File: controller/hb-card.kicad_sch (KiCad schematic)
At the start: 12 parts, among them J4 Conn_01x14

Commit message: Controller - More work mainly on layout
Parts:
- R18, R23, R24, R42, R43, R44, R45, R46: footprint Resistor_SMD:R_0402_1005Metric -> Resistor_SMD:R_0805_2012Metric
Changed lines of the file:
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@@
 			)
 		)
-		(property "Footprint" "Resistor_SMD:R_0402_1005Metric"
+		(property "Footprint" "Resistor_SMD:R_0805_2012Metric"
 			(at 77.47 90.17 0)
 			(effects
@@
 			)
 		)
-		(property "Footprint" "Resistor_SMD:R_0402_1005Metric"
+		(property "Footprint" "Resistor_SMD:R_0805_2012Metric"
 			(at 77.47 95.25 0)
 			(effects
@@
 			)
 		)
-		(property "Footprint" "Resistor_SMD:R_0402_1005Metric"
+		(property "Footprint" "Resistor_SMD:R_0805_2012Metric"
 			(at 77.47 67.31 0)
 			(effects
@@
 			)
 		)
-		(property "Footprint" "Resistor_SMD:R_0402_1005Metric"
+		(property "Footprint" "Resistor_SMD:R_0805_2012Metric"
 			(at 77.47 59.69 0)
 			(effects
@@
 			)
 		)
-		(property "Footprint" "Resistor_SMD:R_0402_1005Metric"
+		(property "Footprint" "Resistor_SMD:R_0805_2012Metric"
 			(at 77.47 62.23 0)
 			(effects
@@
 			)
 		)
-		(property "Footprint" "Resistor_SMD:R_0402_1005Metric"
+		(property "Footprint" "Resistor_SMD:R_0805_2012Metric"
 			(at 77.47 92.71 0)
 			(effects
@@
 			)
 		)
-		(property "Footprint" "Resistor_SMD:R_0402_1005Metric"
+		(property "Footprint" "Resistor_SMD:R_0805_2012Metric"
 			(at 77.47 87.63 0)
 			(effects
@@
 			)
 		)
-		(property "Footprint" "Resistor_SMD:R_0402_1005Metric"
+		(property "Footprint" "Resistor_SMD:R_0805_2012Metric"
 			(at 77.47 64.77 0)
 			(effects

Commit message: Controller - some more changes
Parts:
- added C38, C43, C48: 10nF, Capacitor_SMD:C_0402_1005Metric, symbol Device:C_Small
- added C53, C58: 1nF 100VDC, Capacitor_SMD:C_0603_1608Metric, symbol Device:C_Small
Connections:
- net Current_sense_xA: now also C43.1
- net Current_sense_xB: now also C38.1
- net Earth: now also C38.2, C43.2, C48.2, C53.2, C58.2
- net FB_x_FULL_HI: now also C53.1
- net FB_x_FULL_LO: now also C58.1
- net NTC_x: now also C48.1

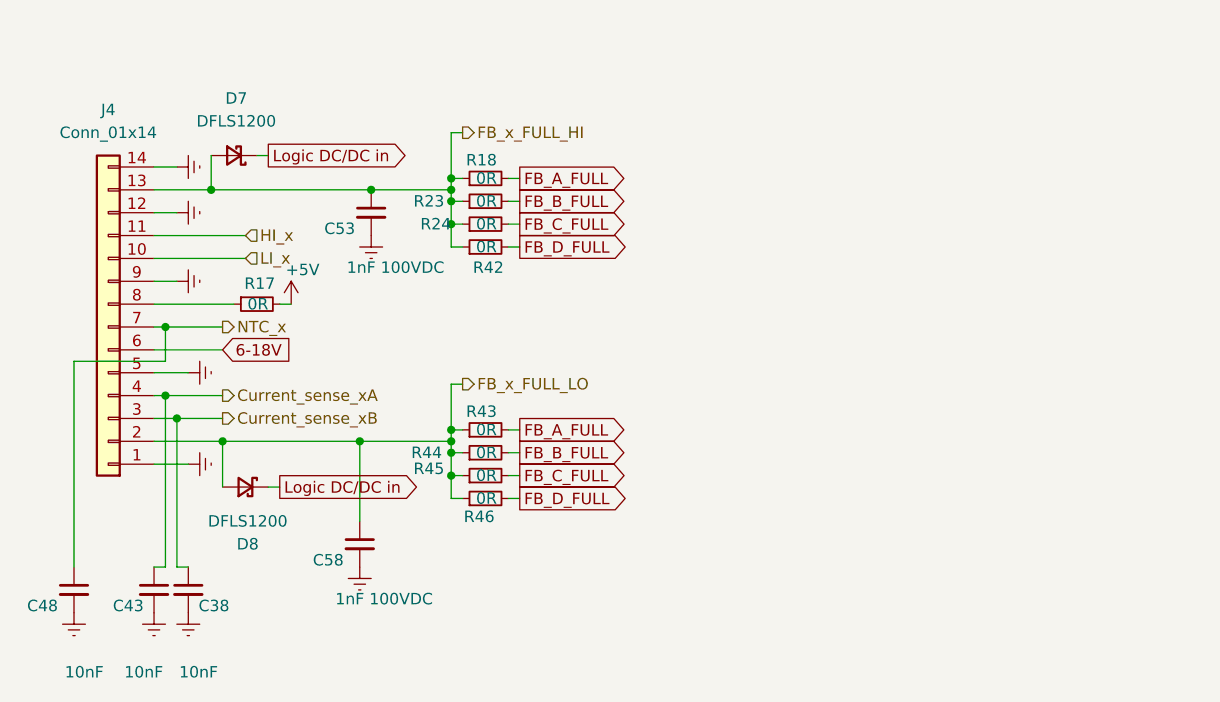
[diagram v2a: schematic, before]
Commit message: Controller - Start work on vbus connection, improve rgb-led placement
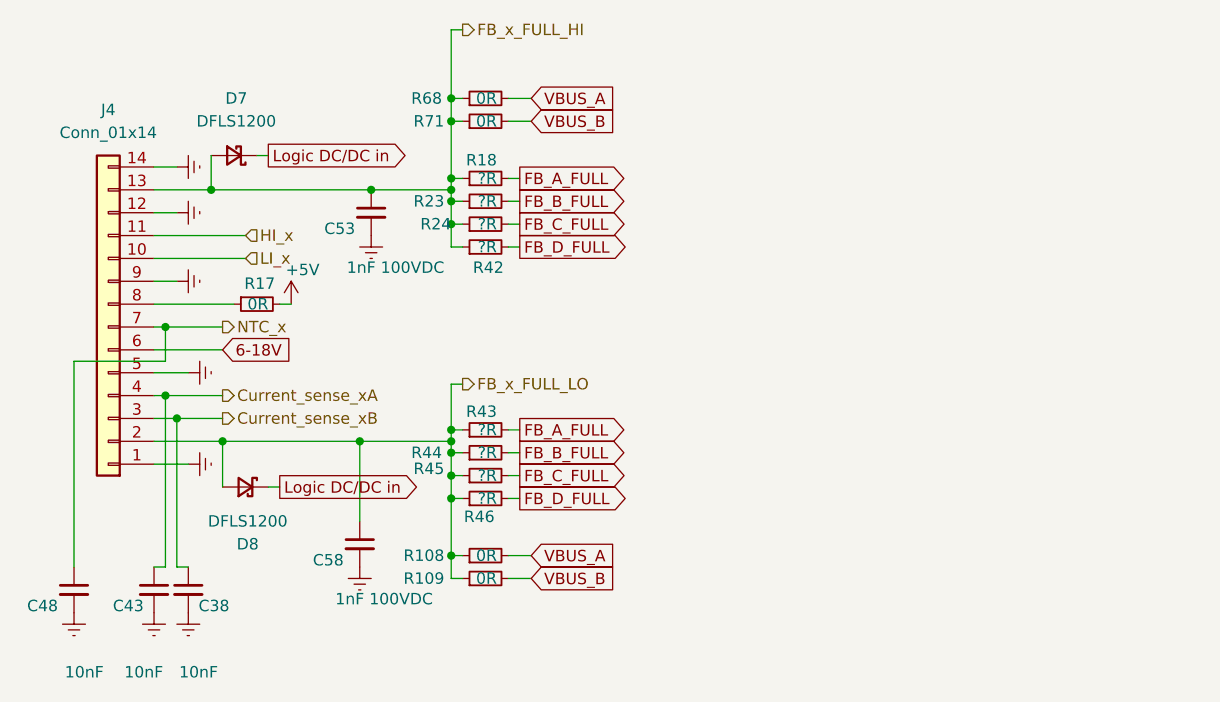
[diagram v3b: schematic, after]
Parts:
- added R108, R109, R68, R71: 0R, Resistor_SMD:R_0805_2012Metric, symbol Device:R_Small
- R18, R23, R24, R42, R43, R44, R45, R46: value 0R -> ?R
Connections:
- net FB_x_FULL_HI: now also R68.1, R71.1
- net FB_x_FULL_LO: now also R108.1, R109.1
- new net VBUS_A: R108.2, R68.2
- new net VBUS_B: R109.2, R71.2

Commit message: Controller - Change current sensor
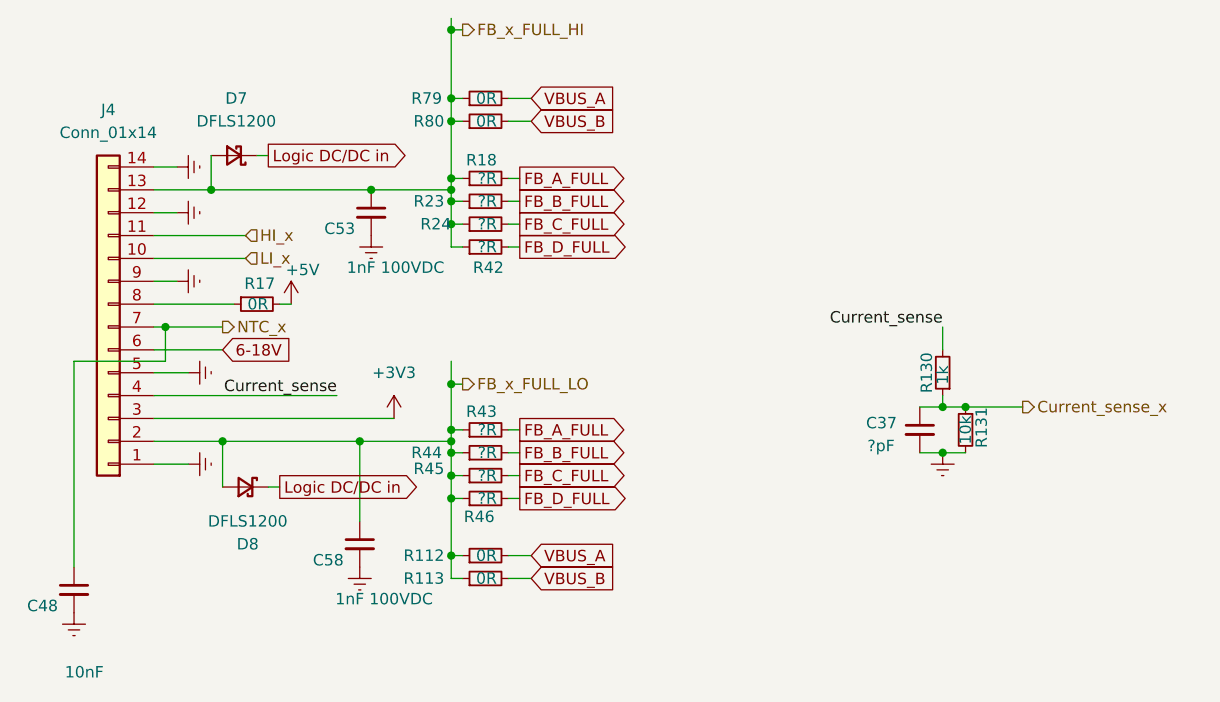
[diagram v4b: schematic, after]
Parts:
- removed C38, C43: 10nF, Capacitor_SMD:C_0402_1005Metric, symbol Device:C_Small
- added C37: ?pF, Capacitor_SMD:C_0402_1005Metric, symbol Device:C_Small
- added R130: 1k, Resistor_SMD:R_0402_1005Metric, symbol Device:R_Small
- added R131: 10k, Resistor_SMD:R_0402_1005Metric, symbol Device:R_Small
- renumbered R108 to R112, R109 to R113, R68 to R79, R71 to R80
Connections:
- net Earth: now also C37.2, R131.2
- net Current_sense_xA renamed Current_sense
- net Current_sense: now also R130.2
- net Current_sense_xB renamed +3V3
- new net Current_sense_x: C37.1, R130.1, R131.1

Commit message: Controller - More routing
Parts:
- removed R131: 10k, Resistor_SMD:R_0402_1005Metric, symbol Device:R_Small
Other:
- moved on the sheet: C37
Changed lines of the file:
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@@
 	)
 	(junction
-		(at 128.27 90.17)
-		(diameter 0)
-		(color 0 0 0 0)
-	)
-	(junction
 		(at 73.66 92.71)
 		(diameter 0)
@@
 	)
 	(junction
-		(at 130.81 85.09)
-		(diameter 0)
-		(color 0 0 0 0)
-	)
-	(junction
 		(at 128.27 85.09)
 		(diameter 0)
@@
 	(wire
 		(pts
-			(xy 128.27 85.09) (xy 130.81 85.09)
+			(xy 128.27 85.09) (xy 137.16 85.09)
 		)
 		(stroke
@@
 	(wire
 		(pts
-			(xy 125.73 90.17) (xy 128.27 90.17)
-		)
-		(stroke
-			(width 0)
-			(type default)
-		)
-	)
-	(wire
-		(pts
 			(xy 74.93 92.71) (xy 73.66 92.71)
 		)
@@
 	(wire
 		(pts
-			(xy 130.81 85.09) (xy 137.16 85.09)
-		)
-		(stroke
-			(width 0)
-			(type default)
-		)
-	)
-	(wire
-		(pts
 			(xy 73.66 87.63) (xy 73.66 88.9)
 		)
@@
 	(wire
 		(pts
-			(xy 125.73 85.09) (xy 128.27 85.09)
-		)
-		(stroke
-			(width 0)
-			(type default)
-		)
-	)
-	(wire
-		(pts
 			(xy 74.93 43.18) (xy 73.66 43.18)
 		)
@@
 	(wire
 		(pts
-			(xy 128.27 90.17) (xy 130.81 90.17)
-		)
-		(stroke
-			(width 0)
-			(type default)
-		)
-	)
-	(wire
-		(pts
 			(xy 73.66 41.91) (xy 73.66 43.18)
 		)
@@
 	(symbol
 		(lib_id "Device:C_Small")
-		(at 125.73 87.63 0)
+		(at 128.27 87.63 0)
 		(unit 1)
 		(exclude_from_sim no)
@@
 		(dnp no)
 		(property "Reference" "C37"
-			(at 123.19 86.868 0)
+			(at 125.73 86.868 0)
 			(effects
 				(font
@@
 		)
 		(property "Value" "?pF"
-			(at 122.936 89.408 0)
+			(at 125.476 89.408 0)
 			(effects
 				(font
@@
 		)
 		(property "Footprint" "Capacitor_SMD:C_0402_1005Metric"
-			(at 125.73 87.63 0)
+			(at 128.27 87.63 0)
 			(effects
 				(font
@@
 		)
 		(property "Datasheet" "~"
-			(at 125.73 87.63 0)
+			(at 128.27 87.63 0)
 			(effects
 				(font
@@
 		)
 		(property "Description" "Unpolarized capacitor, small symbol"
-			(at 125.73 87.63 0)
+			(at 128.27 87.63 0)
 			(effects
 				(font
@@
 					(unit 1)
 				)
-			)
-		)
-	)
-	(symbol
-		(lib_id "Device:R_Small")
-		(at 130.81 87.63 0)
-		(mirror y)
-		(unit 1)
-		(exclude_from_sim no)
-		(in_bom yes)
-		(on_board yes)
-		(dnp no)
-		(property "Reference" "R131"
-			(at 132.588 87.376 90)
-			(effects
-				(font
-					(size 1.27 1.27)
-				)
-			)
-		)
-		(property "Value" "10k"
-			(at 130.81 87.63 90)
-			(effects
-				(font
-					(size 1.27 1.27)
-				)
-			)
-		)
-		(property "Footprint" "Resistor_SMD:R_0402_1005Metric"
-			(at 130.81 87.63 0)
-			(effects
-				(font
-					(size 1.27 1.27)
-				)
-				(hide yes)
-			)
-		)
-		(property "Datasheet" "~"
-			(at 130.81 87.63 0)
-			(effects
-				(font
-					(size 1.27 1.27)
-				)
-				(hide yes)
-			)
-		)
-		(property "Description" "Resistor, small symbol"
-			(at 130.81 87.63 0)
-			(effects
-				(font
-					(size 1.27 1.27)
-				)
-				(hide yes)
-			)
-		)
-		(pin "1"
-		)
-		(pin "2"
-		)
-		(instances
-			(project "controller"
-				(path "/5b092a03-7e3e-4df1-ad91-2ac0e362f857/841b52a4-3318-4fac-b55e-9de2ad4fe4ee"
-					(reference "R131")
-					(unit 1)
-				)
-				(path "/5b092a03-7e3e-4df1-ad91-2ac0e362f857/862e8064-9f06-4505-bb2d-3efa3044593e"
-					(reference "R133")
-					(unit 1)
-				)
-				(path "/5b092a03-7e3e-4df1-ad91-2ac0e362f857/9f4be3a6-fd4f-491e-be65-69cf4b3ed547"
-					(reference "R123")
-					(unit 1)
-				)
-				(path "/5b092a03-7e3e-4df1-ad91-2ac0e362f857/b6f7c2c4-d7db-44b7-b030-eb8c4bb9e571"
-					(reference "R129")
-					(unit 1)
-				)
-				(path "/5b092a03-7e3e-4df1-ad91-2ac0e362f857/b9c56faa-c91b-4a56-a1ba-01961aa6f4f8"
-					(reference "R135")
-					(unit 1)
-				)
